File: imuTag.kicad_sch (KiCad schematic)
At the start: 32 parts, among them J1 Conn_02x05_Odd_Even, J3 Conn_01x02_Pin, Q1 DMG2305UX-13, U1 E73-2G4M08S1C, U2 ME6211C30M5G-N, U3 GD25Q64ESIG, Y2 Crystal

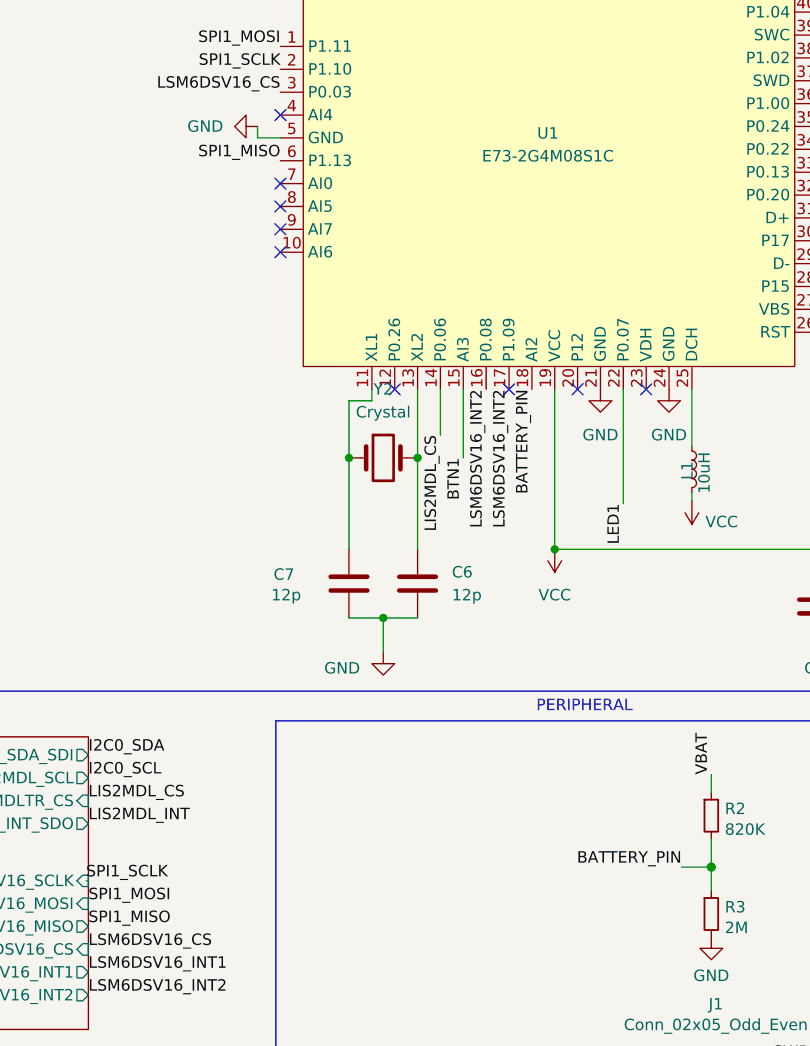
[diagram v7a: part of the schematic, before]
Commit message: Add debug pins AI0 to AI4 to layout
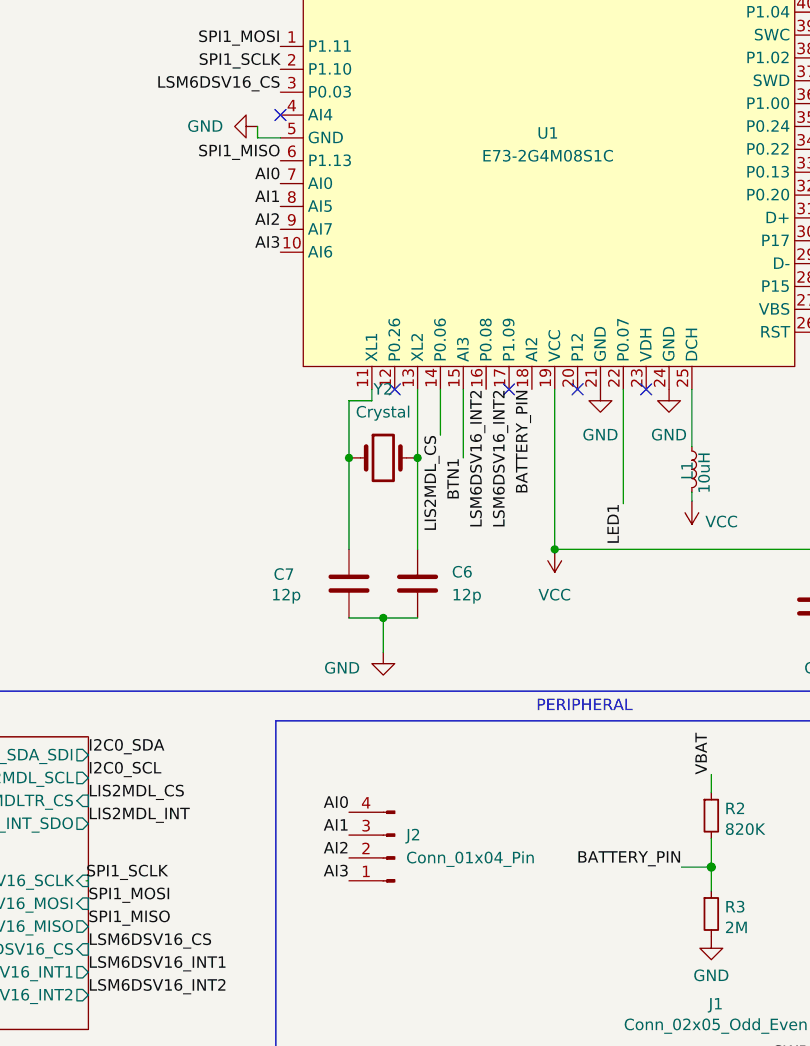
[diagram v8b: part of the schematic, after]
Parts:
- added J2: Conn_01x04_Pin, Connector_PinHeader_2.54mm:PinHeader_1x04_P2.54mm_Vertical, symbol Connector:Conn_01x04_Pin
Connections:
- net AI3: now reaches U1.10 (AI6)
- net AI3: now also J2.1 (Pin_1)
- net AI0: now reaches U1.7 (AI0)
- net AI0: now also J2.4 (Pin_4)
- net AI1: now reaches U1.8 (AI5)
- net AI1: now also J2.3 (Pin_3)
- net AI2: now reaches U1.9 (AI7)
- net AI2: now also J2.2 (Pin_2)
- no-connect marks 22 -> 18
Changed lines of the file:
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@@
 	)
 	(no_connect
-		(at 180.34 54.61)
-	)
-	(no_connect
 		(at 240.03 20.32)
 	)
 	(no_connect
-		(at 180.34 46.99)
-	)
-	(no_connect
 		(at 193.04 69.85)
 	)
@@
 	)
 	(no_connect
-		(at 180.34 52.07)
-	)
-	(no_connect
 		(at 235.077 149.606)
 	)
@@
 	)
 	(no_connect
-		(at 180.34 49.53)
-	)
-	(no_connect
 		(at 80.01 101.6)
 	)
@@
 		)
 	)
+	(label "AI2"
+		(at 180.34 52.07 180)
+		(effects
+			(font
+				(size 1.27 1.27)
+			)
+			(justify right bottom)
+		)
+	)
 	(label "I2C0_SCL"
 		(at 240.03 22.86 0)
@@
 		)
 	)
+	(label "AI0"
+		(at 187.96 116.84 180)
+		(effects
+			(font
+				(size 1.27 1.27)
+			)
+			(justify right bottom)
+		)
+	)
 	(label "QSPI_IO1"
 		(at 240.03 48.26 0)
@@
 		)
 	)
+	(label "AI2"
+		(at 187.96 121.92 180)
+		(effects
+			(font
+				(size 1.27 1.27)
+			)
+			(justify right bottom)
+		)
+	)
 	(label "USB_D+"
 		(at 240.03 50.8 0)
@@
 		)
 	)
+	(label "AI3"
+		(at 180.34 54.61 180)
+		(effects
+			(font
+				(size 1.27 1.27)
+			)
+			(justify right bottom)
+		)
+	)
 	(label "BTN1"
 		(at 269.24 139.7 0)
@@
 		)
 	)
+	(label "AI1"
+		(at 187.96 119.38 180)
+		(effects
+			(font
+				(size 1.27 1.27)
+			)
+			(justify right bottom)
+		)
+	)
 	(label "LIS2MDL_CS"
 		(at 159.004 115.57 0)
@@
 		)
 	)
+	(label "AI3"
+		(at 187.96 124.46 180)
+		(effects
+			(font
+				(size 1.27 1.27)
+			)
+			(justify right bottom)
+		)
+	)
 	(label "SPI1_SCLK"
 		(at 180.34 34.29 180)
@@
 		)
 	)
+	(label "AI0"
+		(at 180.34 46.99 180)
+		(effects
+			(font
+				(size 1.27 1.27)
+			)
+			(justify right bottom)
+		)
+	)
 	(label "LSM6DSV16_CS"
 		(at 159.004 132.08 0)
@@
 		)
 	)
+	(label "AI1"
+		(at 180.34 49.53 180)
+		(effects
+			(font
+				(size 1.27 1.27)
+			)
+			(justify right bottom)
+		)
+	)
 	(label "VBAT"
 		(at 24.1094 124.46 0)
@@
 					(unit 1)
 				)
+			)
+		)
+	)
+	(symbol
+		(lib_id "Connector:Conn_01x04_Pin")
+		(at 193.04 121.92 180)
+		(unit 1)
+		(exclude_from_sim no)
+		(in_bom yes)
+		(on_board yes)
+		(dnp no)
+		(fields_autoplaced yes)
+		(property "Reference" "J2"
+			(at 194.31 119.3799 0)
+			(effects
+				(font
+					(size 1.27 1.27)
+				)
+				(justify right)
+			)
+		)
+		(property "Value" "Conn_01x04_Pin"
+			(at 194.31 121.9199 0)
+			(effects
+				(font
+					(size 1.27 1.27)
+				)
+				(justify right)
+			)
+		)
+		(property "Footprint" "Connector_PinHeader_2.54mm:PinHeader_1x04_P2.54mm_Vertical"
+			(at 193.04 121.92 0)
+			(effects
+				(font
+					(size 1.27 1.27)
+				)
+				(hide yes)
+			)
+		)
+		(property "Datasheet" "~"
+			(at 193.04 121.92 0)
+			(effects
+				(font
+					(size 1.27 1.27)
+				)
+				(hide yes)
+			)
+		)
+		(property "Description" "Generic connector, single row, 01x04, script generated"
+			(at 193.04 121.92 0)
+			(effects
+				(font
+					(size 1.27 1.27)
+				)
+				(hide yes)
+			)
+		)
+		(pin "1"
+		)
+		(pin "3"
+		)
+		(pin "2"
+		)
+		(pin "4"
+		)
+		(instances
+			(project ""
+				(path "/b0790ebf-2d8c-4cec-b4ed-465f5b1bb1fd"
+					(reference "J2")
+					(unit 1)
+				)
